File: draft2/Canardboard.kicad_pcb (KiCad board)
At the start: 2 copper layers, 77 parts, among them J1 RBUS, J2 USB_C_Receptacle_USB2.0, U1 ESP32-S3, U2 SN65HVD230, U5 LM66100, U6 LM66100, U7 MAX77827AEFD+T, U8 SC4215, Y1 40MHz±10ppm

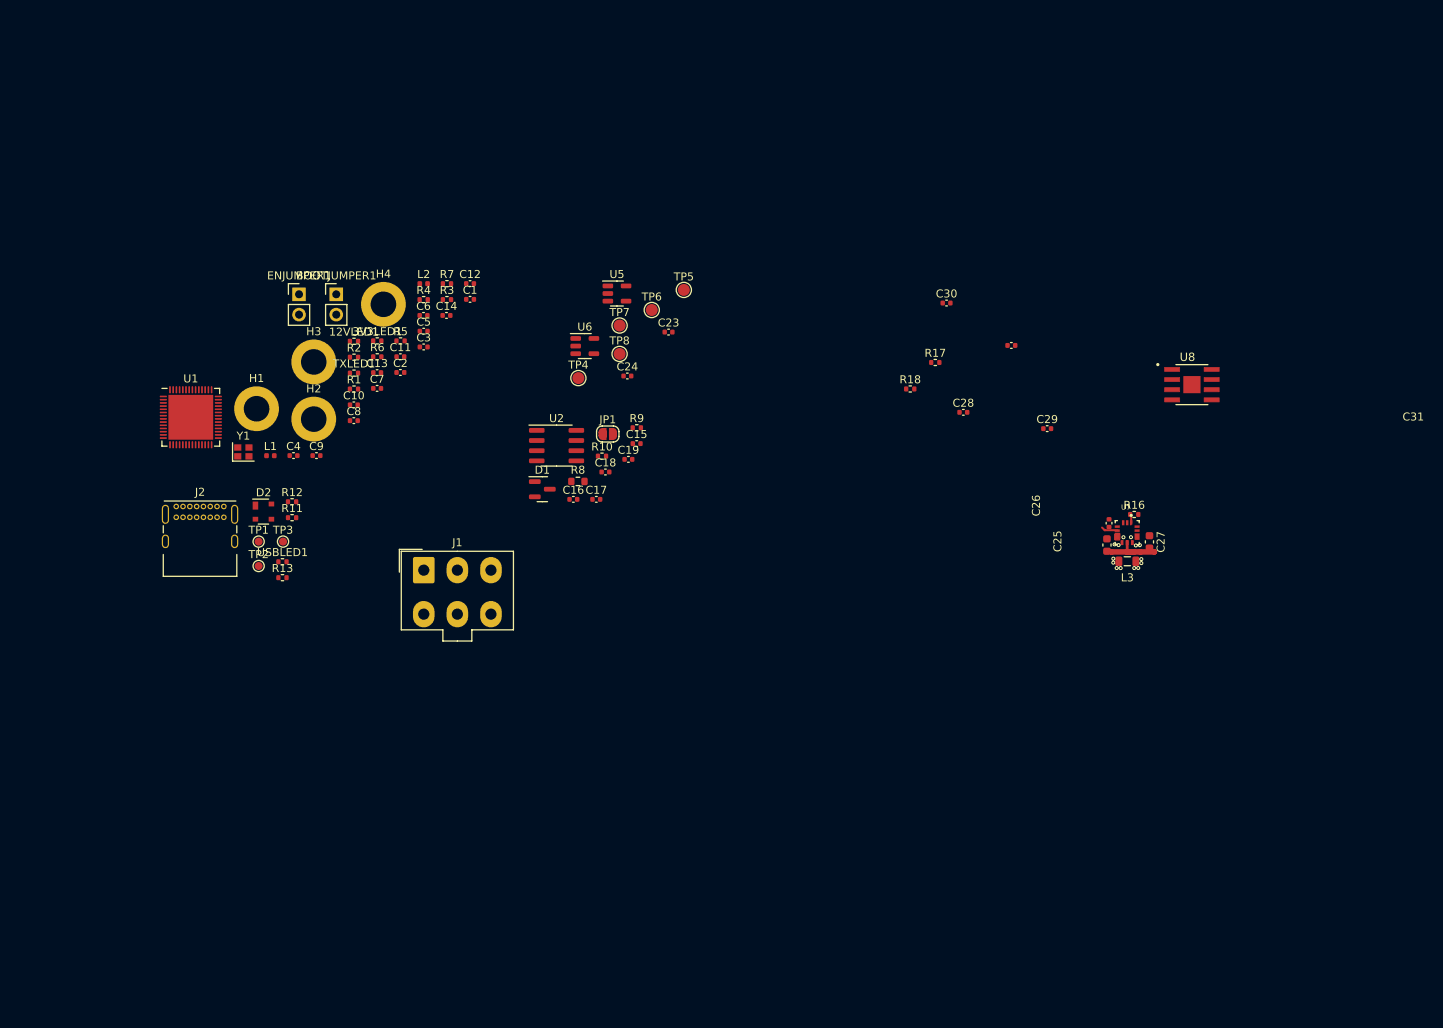
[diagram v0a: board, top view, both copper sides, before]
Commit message: pcb roughly organized
andrei updated his board agaain
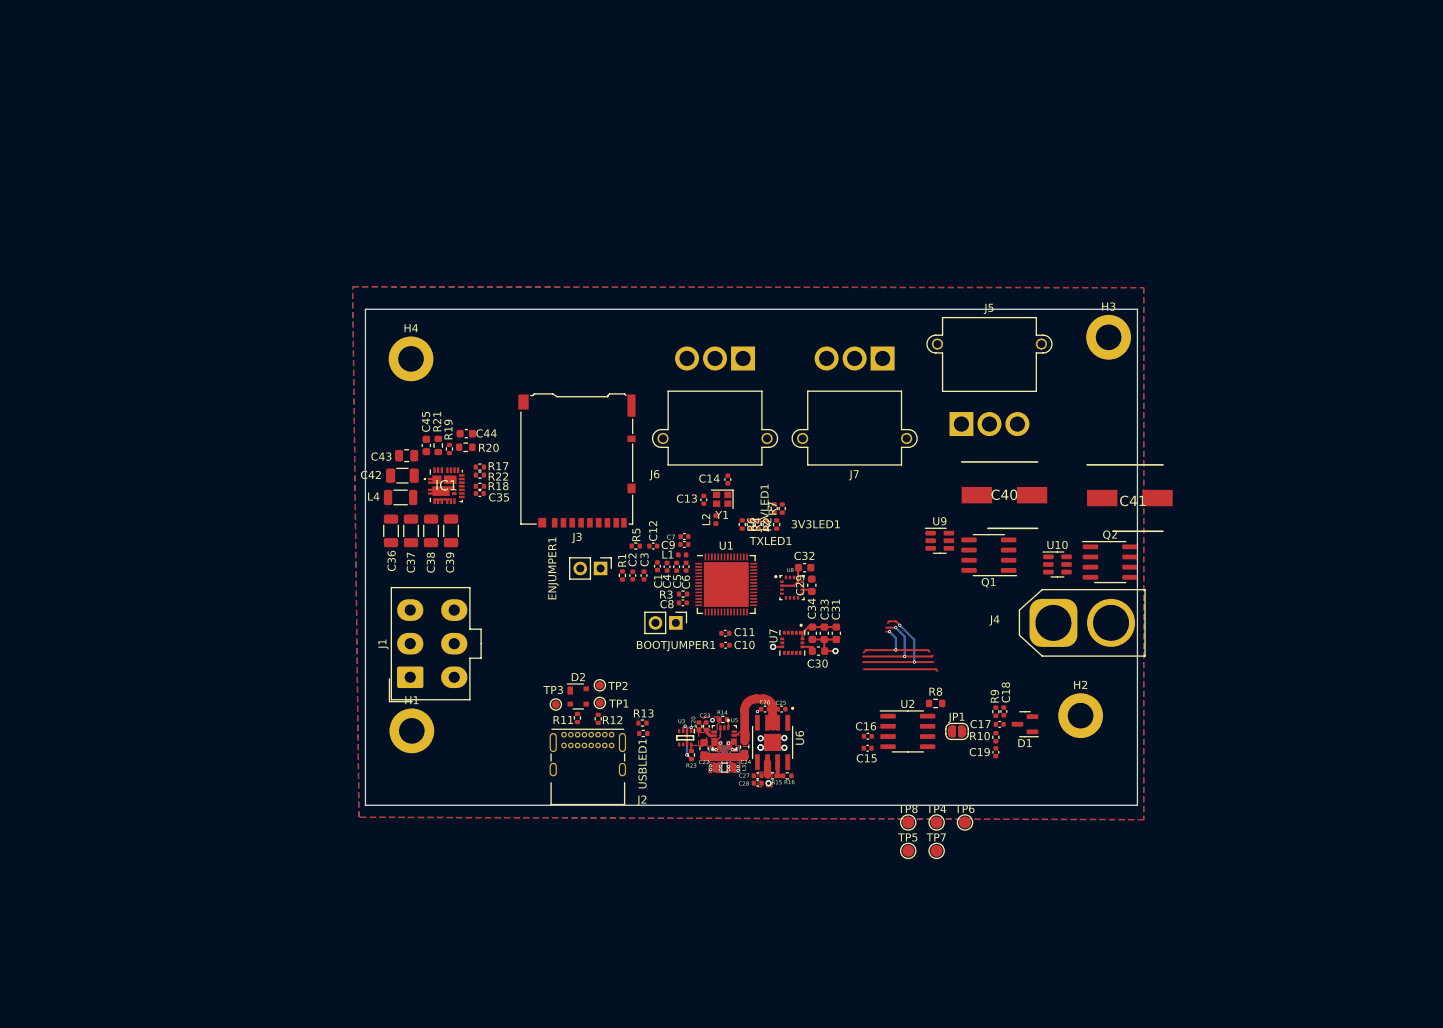
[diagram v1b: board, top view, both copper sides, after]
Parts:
- added C20: 10uF, Capacitor_SMD:C_0402_1005Metric, F.Cu at (121.5, 114.2)
- added C22: 10uF, Capacitor_SMD:C_0603_1608Metric, F.Cu at (122.1, 117.0)
- added C32: 1uF, Capacitor_SMD:C_0603_1608Metric, F.Cu at (134.7, 94.4)
- added C33: 0.1uF, Capacitor_SMD:C_0603_1608Metric, F.Cu at (137.2, 102.6)
- added C34: 2.2uF, Capacitor_SMD:C_0603_1608Metric, F.Cu at (135.7, 102.6)
- added C35: 4.7uF, Capacitor_SMD:C_0402_1005Metric, F.Cu at (94.1, 85.1)
- added C36: 47uF, Capacitor_SMD:C_1206_3216Metric, F.Cu at (83.0, 89.8)
- added C37: 47uF, Capacitor_SMD:C_1206_3216Metric, F.Cu at (85.5, 89.8)
- added C38: 47uF, Capacitor_SMD:C_1206_3216Metric, F.Cu at (88.0, 89.8)
- added C39: 47uF, Capacitor_SMD:C_1206_3216Metric, F.Cu at (90.5, 89.8)
- added C40: 106uF, iclr:CAPAE830X1050N, F.Cu at (159.7, 85.3)
- added C41: 106uF, iclr:CAPAE830X1050N, F.Cu at (175.3, 85.7)
- added C42: 22uF, Capacitor_SMD:C_1206_3216Metric, F.Cu at (84.4, 82.9)
- added C43: 100nF, Capacitor_SMD:C_0805_2012Metric, F.Cu at (85.0, 80.4)
- added C44: 1uF, Capacitor_SMD:C_0603_1608Metric, F.Cu at (92.4, 77.6)
- added C45: 0.1uF, Capacitor_SMD:C_0603_1608Metric, F.Cu at (87.4, 79.1)
- added IC1: SIC437DED-T1-GE3, iclr:SIC437DEDT1GE3, F.Cu at (89.9, 84.1)
- added J3: Micro_SD_Card_Det, Connector_Card:microSD_HC_Hirose_DM3AT-SF-PEJM5, F.Cu at (106.2, 81.1)
- added J4: Conn_01x02_Male, Connector_AMASS:AMASS_XT60-M_1x02_P7.20mm_Vertical, F.Cu at (165.8, 101.3)
- added J5: Conn_01x03_Male, Connector_AMASS:AMASS_MR30PW-M_1x03_P3.50mm_Horizontal, F.Cu at (154.3, 76.4)
- added J6: Conn_01x03_Male, Connector_AMASS:AMASS_MR30PW-M_1x03_P3.50mm_Horizontal, F.Cu at (127.0, 68.2)
- added J7: Conn_01x03_Male, Connector_AMASS:AMASS_MR30PW-M_1x03_P3.50mm_Horizontal, F.Cu at (144.4, 68.2)
- added L4: 1.5uH, Inductor_SMD:L_1206_3216Metric, F.Cu at (84.2, 85.6)
- added Q1: SI4143DY-T1-GE3, Package_SO:SOIC-8_3.9x4.9mm_P1.27mm, F.Cu at (157.7, 92.8)
- added Q2: SI4143DY-T1-GE3, Package_SO:SOIC-8_3.9x4.9mm_P1.27mm, F.Cu at (172.9, 93.7)
- added R14: 14k, Resistor_SMD:R_0402_1005Metric, F.Cu at (124.5, 113.4)
- added R15: 56k, Resistor_SMD:R_0402_1005Metric, F.Cu at (130.7, 120.4)
- added R19: 100k, Resistor_SMD:R_0402_1005Metric, F.Cu at (90.3, 79.6)
- added R20: 499k, Resistor_SMD:R_0603_1608Metric, F.Cu at (92.3, 79.3)
- added R21: 2.2, Resistor_SMD:R_0603_1608Metric, F.Cu at (88.9, 79.1)
- added R22: 10k, Resistor_SMD:R_0402_1005Metric, F.Cu at (94.1, 82.8)
- added R23: 10k, Resistor_SMD:R_0402_1005Metric, F.Cu at (120.5, 117.8)
- added U10: LTC4412xS6, Package_TO_SOT_SMD:TSOT-23-6, F.Cu at (166.3, 94.0)
- added U3: LM66200DRLR, iclr:SOTFL50P160X60-8N, F.Cu at (119.8, 115.7)
- added U9: LTC4412xS6, Package_TO_SOT_SMD:TSOT-23-6, F.Cu at (151.6, 91.0)
- C23: value 4.7uF -> 1uF
- C24: value 4.7uF -> 22uF; footprint Capacitor_SMD:C_0402_1005Metric -> Capacitor_SMD:C_0603_1608Metric
- C25: footprint Capacitor_SMD:C_0603_1608Metric -> Capacitor_SMD:C_0402_1005Metric
- C26: value 1uF -> 4.7uF
- C27: value 22uF -> 10uF; footprint Capacitor_SMD:C_0603_1608Metric -> Capacitor_SMD:C_0402_1005Metric
- C28: value 10uF -> 0.1uF
- C29: value 4.7uF -> 10uF; footprint Capacitor_SMD:C_0402_1005Metric -> Capacitor_SMD:C_0603_1608Metric
- C30: value 10uF -> 0.47uF; footprint Capacitor_SMD:C_0402_1005Metric -> Capacitor_SMD:C_0603_1608Metric
- C31: value 0.1uF -> 10nF; footprint Capacitor_SMD:C_0402_1005Metric -> Capacitor_SMD:C_0603_1608Metric
- R16: value 14k -> 10k
- R17: value 56k -> 45K
- U5: value LM66100 -> MAX77827AEFD+T; footprint Package_TO_SOT_SMD:SOT-23-5 -> iclr:CONV_MAX77827AEFD+T
- U6: value LM66100 -> SC4215; footprint Package_TO_SOT_SMD:SOT-23-5 -> iclr:SOIC127P599X175-9N
- U7: value MAX77827AEFD+T -> ICM-20608-G; footprint iclr:CONV_MAX77827AEFD+T -> iclr:PQFN50P300X300X80-16N
- U8: value SC4215 -> MMC5983MA; footprint iclr:SOIC127P599X175-9N -> iclr:PQFN50P300X300X100-16N
- moved H2 102.8 mm to (169.2, 112.9)
- moved H3 99.4 mm to (172.7, 65.6)
- moved TP7 76.7 mm to (151.2, 129.8)
- moved TP5 75.5 mm to (147.7, 129.8)
- moved TP6 75.1 mm to (154.8, 126.2)
- moved TP4 71.4 mm to (151.2, 126.2)
- moved U1 70.1 mm to (124.9, 96.5)
- moved TP8 68.8 mm to (147.7, 126.2)
- moved D1 67.1 mm to (162.2, 114.0), turned to 180 degrees
- moved R10 60.5 mm to (158.6, 115.6), turned to -90 degrees
- moved Y1 60.2 mm to (124.4, 85.8), turned to 180 degrees
- moved BOOTJUMPER1 59.1 mm to (118.6, 101.3), turned to -90 degrees
- moved C19 58.7 mm to (158.6, 117.5), turned to 90 degrees
- moved R17 58.4 mm to (94.1, 81.8), turned to 180 degrees
- moved C18 58.1 mm to (159.6, 112.4), turned to 90 degrees
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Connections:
- C23 pad 1: /Power/BBIN -> /Power/BIAS
- C24 pad 1: /Power/BBIN -> /Power/BBOUT
- C25 pad 1: /Power/BBIN -> /Power/BBOUT
- C26 pad 1: /Power/BIAS -> /Power/BBOUT
- C26 pad 2: GNDA -> GND
- C27 pad 1: /Power/BBOUT -> GND
- C27 pad 2: GND -> +3V3
- C28 pad 1: /Power/BBOUT -> GND
- C28 pad 2: GND -> +3V3
- C29 pad 1: /Power/BBOUT -> Net-(C29-Pad1)
- C30 pad 1: GND -> Net-(C30-Pad1)
- C30 pad 2: +3V3 -> GND
- C31 pad 1: GND -> Net-(C31-Pad1)
- C31 pad 2: +3V3 -> GND
- R16 pad 1: /Power/SEL -> /Power/FBIn
- R16 pad 2: GNDA -> GND
- R17 pad 1: +3V3 -> /SERVO_PWR
- R17 pad 2: /Power/FBIn -> /comps/FB1
- R18 pad 1: /Power/FBIn -> /comps/PGOOD
- R18 pad 2: GND -> Net-(C44-Pad1)
- U1 pad 36: unconnected-(U1-Pad36) -> /SERVO_SGNL1
- U1 pad 37: unconnected-(U1-Pad37) -> /SERVO_SGNL2
- U1 pad 38: unconnected-(U1-Pad38) -> /SPI_CLK
- U1 pad 39: unconnected-(U1-Pad39) -> /SPI_MOSI
- U1 pad 40: unconnected-(U1-Pad40) -> /SPI_MISO
- U1 pad 41: unconnected-(U1-Pad41) -> /IMU_CS
- U1 pad 42: unconnected-(U1-Pad42) -> /MAG_CS
- U1 pad 43: unconnected-(U1-Pad43) -> /SD_CS
- U1 pad 44: unconnected-(U1-Pad44) -> /SERVO_SGNL3
- U5 pad 1: RBUS_uC_V -> /Power/SEL
- U5 pad 2: GND -> unconnected-(U5-Pad2)
- U5 pad 3: GND -> /Power/BBIN
- U5 pad 4: unconnected-(U5-Pad4) -> GND
- U5 pad 5: /Power/BBIN -> /Power/BIAS
- U6 pad 1: VBUS -> unconnected-(U6-Pad1)
- U6 pad 2: GND -> /Power/BBOUT
- U6 pad 3: GND -> /Power/BBOUT
- U6 pad 5: /Power/BBIN -> (no net)
- U7 pad 1: /Power/SEL -> Net-(C31-Pad1)
- U7 pad 10: /Power/LX2 -> GND
- U7 pad 11: /Power/BBOUT -> GND
- U7 pad 13: /Power/BBOUT -> GND
- U7 pad 14: unconnected-(U7-Pad14) -> Net-(C30-Pad1)
- U7 pad 2: unconnected-(U7-Pad2) -> /SPI_CLK
- U7 pad 3: /Power/BBIN -> /SPI_MOSI
- U7 pad 4: GNDA -> /SPI_MISO
- U7 pad 5: /Power/BIAS -> /IMU_CS
- U7 pad 6: /Power/BBIN -> unconnected-(U7-Pad6)
- U7 pad 8: /Power/LX1 -> GND
- U8 pad 1: unconnected-(U8-Pad1) -> /SPI_CLK
- U8 pad 2: /Power/BBOUT -> +3V3
- U8 pad 3: /Power/BBOUT -> unconnected-(U8-Pad3)
- U8 pad 4: unconnected-(U8-Pad4) -> /MAG_CS
- U8 pad 5: (no net) -> /SPI_MISO
- U8 pad 6: +3V3 -> unconnected-(U8-Pad6)
- U8 pad 7: /Power/FBIn -> unconnected-(U8-Pad7)
- U8 pad 8: GND -> unconnected-(U8-Pad8)
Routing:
- net GND: track 7.51 -> 64.4 mm, vias 0 -> 15
- net /Power/BBOUT: track 0.00 -> 12.3 mm
- net +3V3: track 0.00 -> 5.61 mm, vias 0 -> 1
- net Net-(C31-Pad1): track 0.00 -> 5.57 mm
- net VBUS: track 0.00 -> 5.27 mm, vias 0 -> 3
- net /Power/BBIN: track 0.00 -> 3.68 mm
- net /Power/FBIn: track 0.00 -> 2.61 mm
- net Net-(C29-Pad1): track 0.00 -> 1.36 mm
- net Net-(C30-Pad1): track 0.00 -> 1.36 mm
- net Net-(R23-Pad2): track 0.00 -> 0.81 mm
- net /Power/BIAS: track 2.08 -> 1.42 mm
- added copper zone on F.Cu, net +3V3
- added copper zone on F.Cu, net /Power/BBOUT
- added copper zone on B.Cu, net /Power/LX1
- added copper zone on F.Cu, net /Power/LX1
- added copper zone on B.Cu, net /Power/LX2
- added copper zone on F.Cu, net /Power/LX2
- added copper zone on B.Cu, net GND
- added copper zone on F.Cu, net GND
- added copper zone on In1.Cu, net GND
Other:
- board outline added: 96.5 x 62 mm
- copper layers 2 -> 4

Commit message: made everything smaller
:)
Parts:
- removed TP3: TestPoint, TestPoint:TestPoint_Pad_D1.0mm
- C40, C41: footprint iclr:CAPAE830X1050N -> Capacitor_SMD:C_0805_2012Metric
- moved TP6 58.7 mm to (102.2, 100.2)
- moved TP5 52.9 mm to (102.2, 102.7)
- moved J3 50.3 mm to (143.3, 115.1), turned to 0 degrees
- moved C15 41.2 mm to (102.1, 109.3)
- moved C17 41.2 mm to (118.6, 106.3)
- moved D1 41.2 mm to (121.8, 106.3)
- moved JP1 41.2 mm to (113.3, 107.2)
- moved C16 41.2 mm to (102.1, 107.8)
- moved C18 41.2 mm to (119.1, 104.7)
- moved C19 41.2 mm to (118.1, 109.8)
- moved R10 41.2 mm to (118.1, 107.9)
- moved R8 41.2 mm to (110.6, 103.7)
- moved R9 41.2 mm to (118.1, 104.7)
- moved U2 41.2 mm to (107.1, 107.2)
- moved R23 40.6 mm to (149.7, 89.6), turned to -90 degrees
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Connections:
- R23 pad 2: (no net) -> Net-(R23-Pad2)
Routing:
- net GND: track 64.4 -> 13.8 mm, vias 15 -> 10
- net VBUS: vias 3 -> 2
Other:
- board size 96.5 x 62 mm -> 63.6 x 48.9 mm

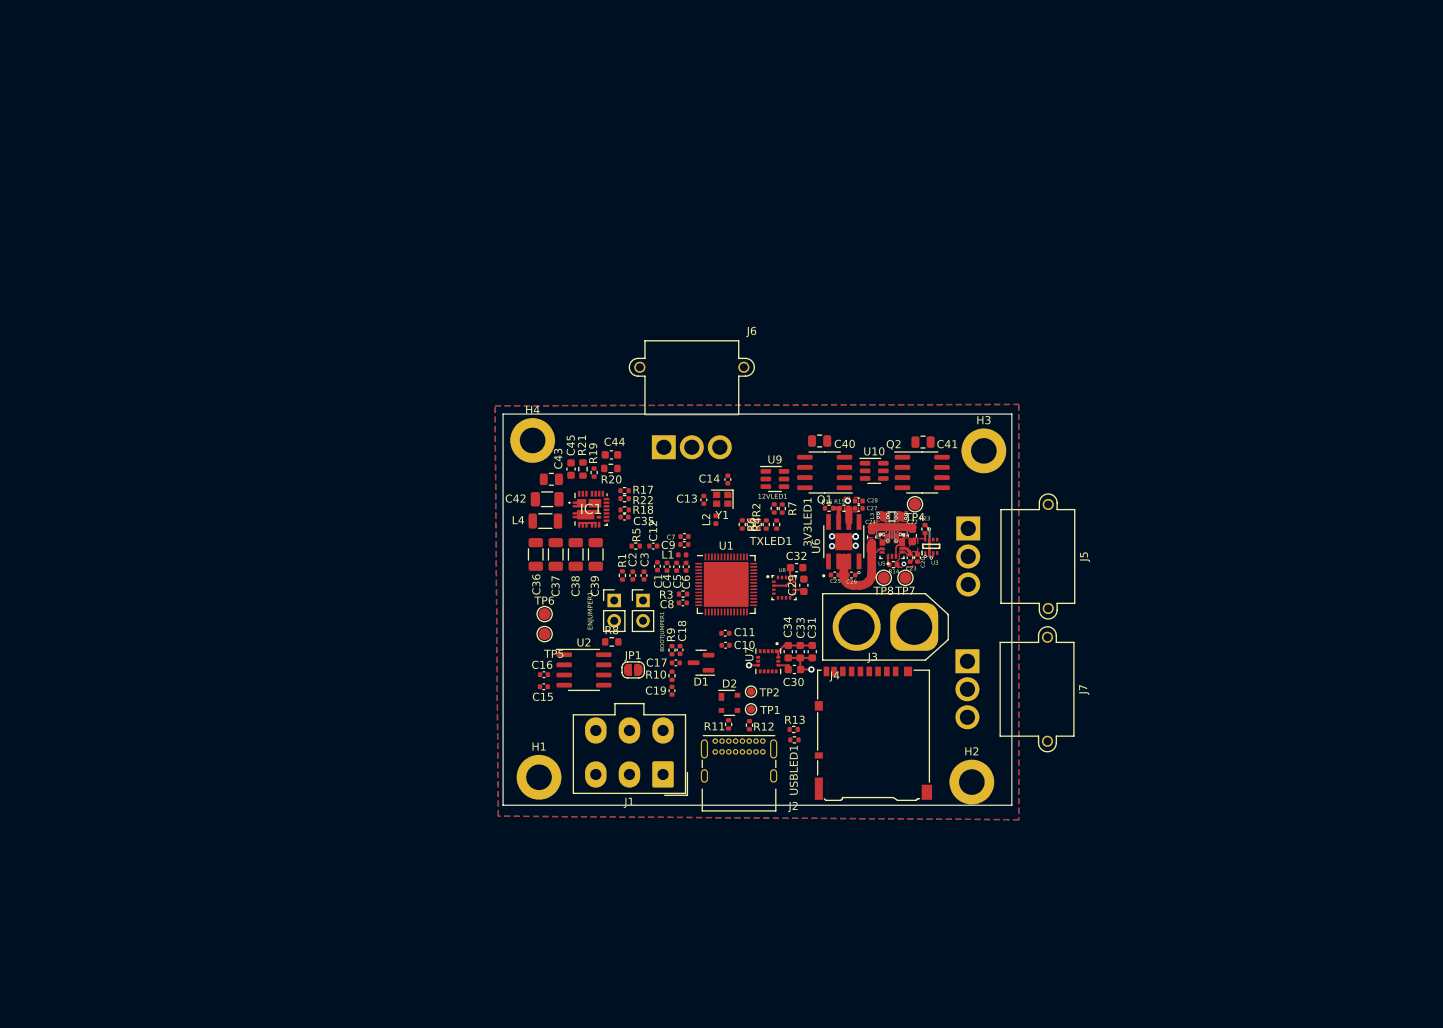
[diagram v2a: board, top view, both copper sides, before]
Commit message: silk screen
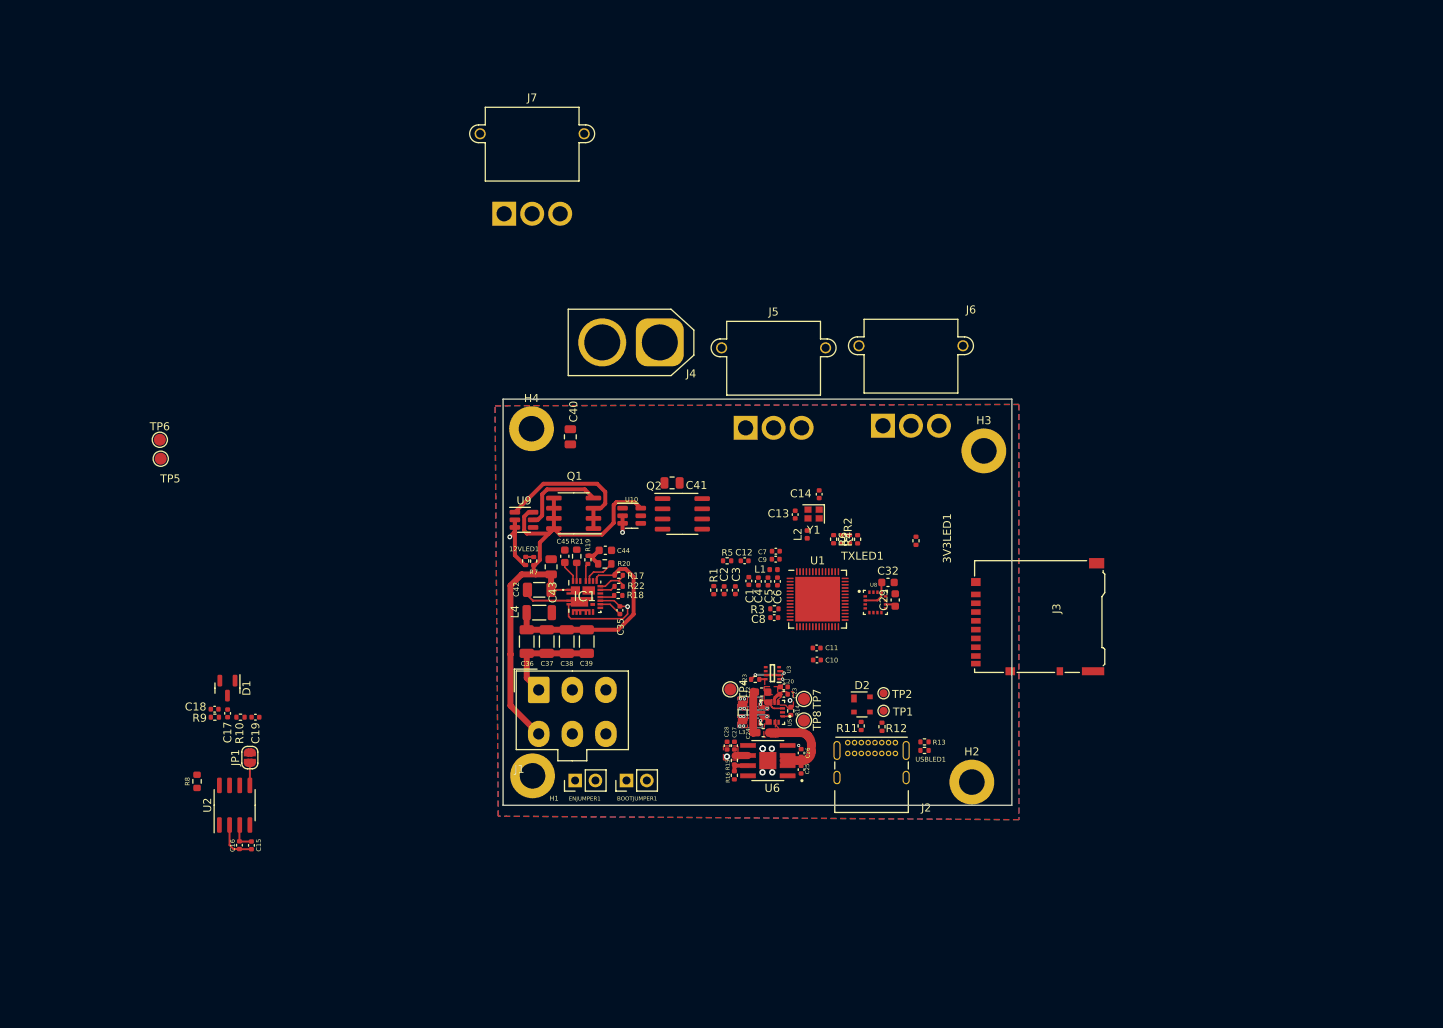
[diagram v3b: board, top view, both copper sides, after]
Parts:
- removed C30: 0.47uF, Capacitor_SMD:C_0603_1608Metric
- removed C31: 10nF, Capacitor_SMD:C_0603_1608Metric
- removed C33: 0.1uF, Capacitor_SMD:C_0603_1608Metric
- removed C34: 2.2uF, Capacitor_SMD:C_0603_1608Metric
- removed U7: ICM-20608-G, iclr:PQFN50P300X300X80-16N
- moved J7 80.5 mm to (97.1, 50.1), turned to 0 degrees
- moved D1 59.3 mm to (62.5, 109.4), turned to -90 degrees
- moved C18 58.6 mm to (61.0, 112.1), turned to 180 degrees
- moved R9 57.8 mm to (61.0, 113.1), turned to 0 degrees
- moved C17 56.4 mm to (62.6, 112.6), turned to 90 degrees
- moved R8 54.7 mm to (58.8, 121.1), turned to -90 degrees
- moved R10 54.2 mm to (64.2, 113.1), turned to 0 degrees
- moved TP6 52.8 mm to (54.1, 78.4)
- moved TP5 52.8 mm to (54.2, 80.8)
- moved C19 52.2 mm to (66.0, 113.1), turned to 180 degrees
- moved JP1 49.2 mm to (65.3, 118.1), turned to 90 degrees
- moved J4 47.7 mm to (116.6, 66.2)
- moved U2 46.8 mm to (63.5, 124.1), turned to 90 degrees
- moved C16 43.6 mm to (64.0, 129.1), turned to -90 degrees
- moved C15 41.6 mm to (65.5, 129.1), turned to -90 degrees
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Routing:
- net +12V: track 0.00 -> 62.8 mm
- net GND: track 13.8 -> 56.6 mm, vias 10 -> 11
- net /SERVO_PWR: track 0.00 -> 27.5 mm
- net /comps/RBUS_16V: track 0.00 -> 19.3 mm
- net Net-(Q1-Pad4): track 0.00 -> 11.1 mm
- net Net-(C31-Pad1): track 5.57 -> 0.00 mm
- net Net-(C44-Pad1): track 0.00 -> 5.21 mm
- net /comps/FB1: track 0.00 -> 4.41 mm
- net /comps/MODE2_1: track 0.00 -> 3.97 mm
- net +3V3: track 5.61 -> 9.18 mm
- net /comps/VDRV: track 0.00 -> 2.96 mm
- net /CAN-BUS/Vref: track 0.00 -> 2.83 mm
- net Net-(C45-Pad1): track 0.00 -> 2.74 mm
- net GNDA: track 0.00 -> 1.96 mm
- net Net-(IC1-Pad23): track 0.00 -> 1.90 mm
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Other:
- board size 63.6 x 48.9 mm -> 63.6 x 50.8 mm

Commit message: Update Canardboard.kicad_pcb
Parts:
- moved R5 7.03 mm to (132.0, 92.7), turned to 90 degrees
- moved C12 3.81 mm to (130.9, 92.7), turned to -90 degrees
- moved C9 2.52 mm to (133.6, 93.2)
- moved C7 2.51 mm to (133.6, 92.2)
- moved C2 0.50 mm to (125.1, 97.1)
- moved C3 0.50 mm to (126.5, 97.1)
- moved R1 0.50 mm to (123.8, 97.1)
- moved C1 0.43 mm to (128.1, 96.2)
- moved C4 0.29 mm to (129.2, 96.2)
- moved C5 0.15 mm to (130.3, 96.1)
- moved L1 0.05 mm to (130.9, 94.6)
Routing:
- net +3V3: track 9.18 -> 27.7 mm
- net /CHIP_PU: track 0.00 -> 10.3 mm
- net GND: track 56.6 -> 65.0 mm
- net Net-(C12-Pad2): track 0.00 -> 3.99 mm
- net Net-(C6-Pad1): track 0.00 -> 3.21 mm
- net Net-(C12-Pad1): track 0.00 -> 1.08 mm
